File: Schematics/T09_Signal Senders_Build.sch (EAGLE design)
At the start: 37 parts, among them IC1 7805TV, IC2 7805TV, IC3 ATMEGA328, SW1 UNIT_ID, X1 , Y2 16MHz

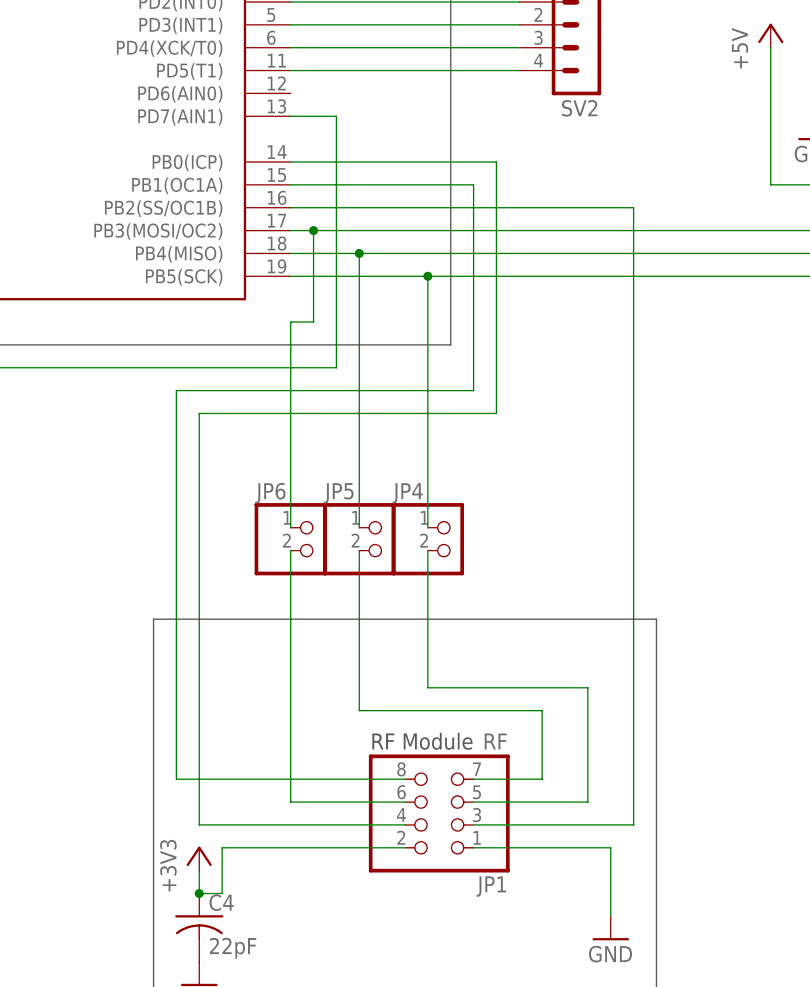
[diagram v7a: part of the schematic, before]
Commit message: Changed RF_SPI Pinout
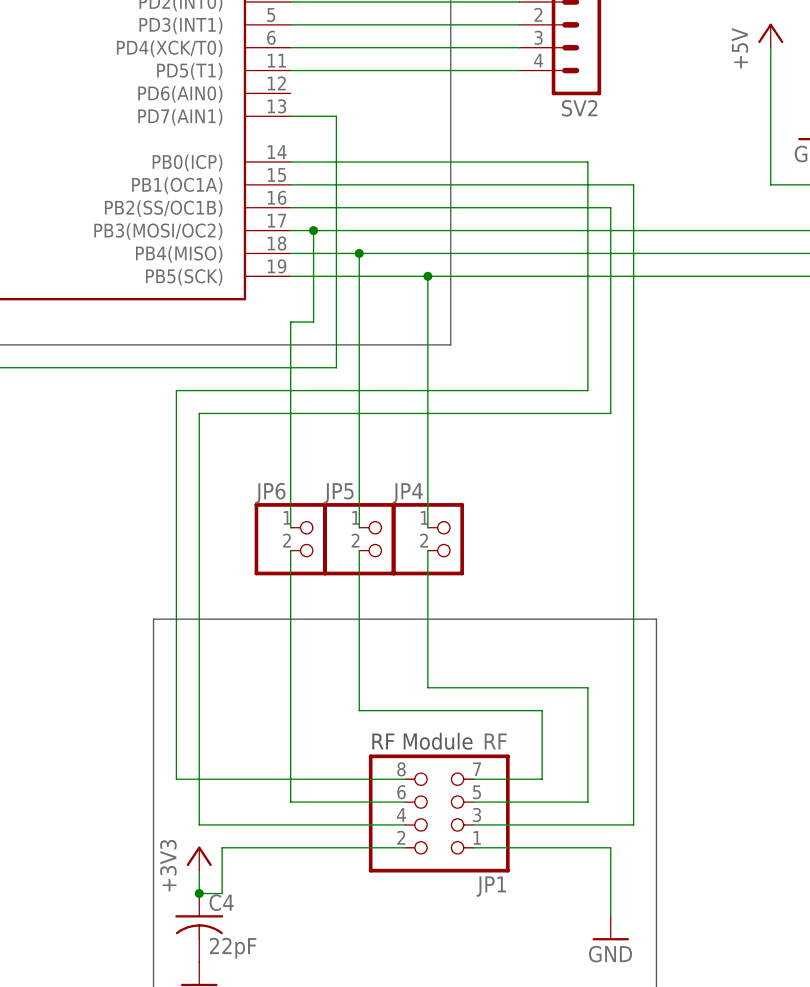
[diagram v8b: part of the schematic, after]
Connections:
- net N$34: now also IC3.PB2(SS/OC1B); no longer IC3.PB0(ICP)
- net N$35: now also IC3.PB0(ICP); no longer IC3.PB1(OC1A)
- net N$36: now also IC3.PB1(OC1A); no longer IC3.PB2(SS/OC1B)
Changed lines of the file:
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@@
 <?xml version="1.0" encoding="utf-8"?>
 <!DOCTYPE eagle SYSTEM "eagle.dtd">
-<eagle version="6.5.0">
+<eagle version="6.3">
 <drawing>
 <settings>
@@
 <wire x1="248.92" y1="30.48" x2="226.06" y2="30.48" width="0.1524" layer="91"/>
 <wire x1="226.06" y1="30.48" x2="226.06" y2="76.2" width="0.1524" layer="91"/>
-<wire x1="226.06" y1="76.2" x2="259.08" y2="76.2" width="0.1524" layer="91"/>
-<wire x1="259.08" y1="76.2" x2="259.08" y2="104.14" width="0.1524" layer="91"/>
-<pinref part="IC3" gate="G$1" pin="PB0(ICP)"/>
-<wire x1="259.08" y1="104.14" x2="236.22" y2="104.14" width="0.1524" layer="91"/>
+<wire x1="226.06" y1="76.2" x2="271.78" y2="76.2" width="0.1524" layer="91"/>
+<wire x1="271.78" y1="76.2" x2="271.78" y2="99.06" width="0.1524" layer="91"/>
+<pinref part="IC3" gate="G$1" pin="PB2(SS/OC1B)"/>
+<wire x1="271.78" y1="99.06" x2="236.22" y2="99.06" width="0.1524" layer="91"/>
 </segment>
 </net>
@@
 <wire x1="248.92" y1="35.56" x2="223.52" y2="35.56" width="0.1524" layer="91"/>
 <wire x1="223.52" y1="35.56" x2="223.52" y2="78.74" width="0.1524" layer="91"/>
-<wire x1="223.52" y1="78.74" x2="256.54" y2="78.74" width="0.1524" layer="91"/>
-<wire x1="256.54" y1="78.74" x2="256.54" y2="101.6" width="0.1524" layer="91"/>
-<pinref part="IC3" gate="G$1" pin="PB1(OC1A)"/>
-<wire x1="256.54" y1="101.6" x2="236.22" y2="101.6" width="0.1524" layer="91"/>
+<wire x1="223.52" y1="78.74" x2="269.24" y2="78.74" width="0.1524" layer="91"/>
+<wire x1="269.24" y1="78.74" x2="269.24" y2="104.14" width="0.1524" layer="91"/>
+<pinref part="IC3" gate="G$1" pin="PB0(ICP)"/>
+<wire x1="269.24" y1="104.14" x2="236.22" y2="104.14" width="0.1524" layer="91"/>
 </segment>
 </net>
 <net name="N$36" class="0">
 <segment>
-<pinref part="IC3" gate="G$1" pin="PB2(SS/OC1B)"/>
-<wire x1="236.22" y1="99.06" x2="274.32" y2="99.06" width="0.1524" layer="91"/>
-<wire x1="274.32" y1="99.06" x2="274.32" y2="30.48" width="0.1524" layer="91"/>
+<wire x1="274.32" y1="101.6" x2="274.32" y2="30.48" width="0.1524" layer="91"/>
 <pinref part="JP1" gate="A" pin="3"/>
 <wire x1="274.32" y1="30.48" x2="256.54" y2="30.48" width="0.1524" layer="91"/>
-</segment>
-</net>
+<pinref part="IC3" gate="G$1" pin="PB1(OC1A)"/>
+<wire x1="236.22" y1="101.6" x2="274.32" y2="101.6" width="0.1524" layer="91"/>
+</segment>
+</net>
